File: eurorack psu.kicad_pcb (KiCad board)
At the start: 2 copper layers, 100 x 60 mm, 27 parts, among them J1 Screw Terminal 1x3, J2 Screw_Terminal_01x03, M3 MountingHole_3.2mm_M3_DIN965_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, U1 LM7812, U2 LM7912

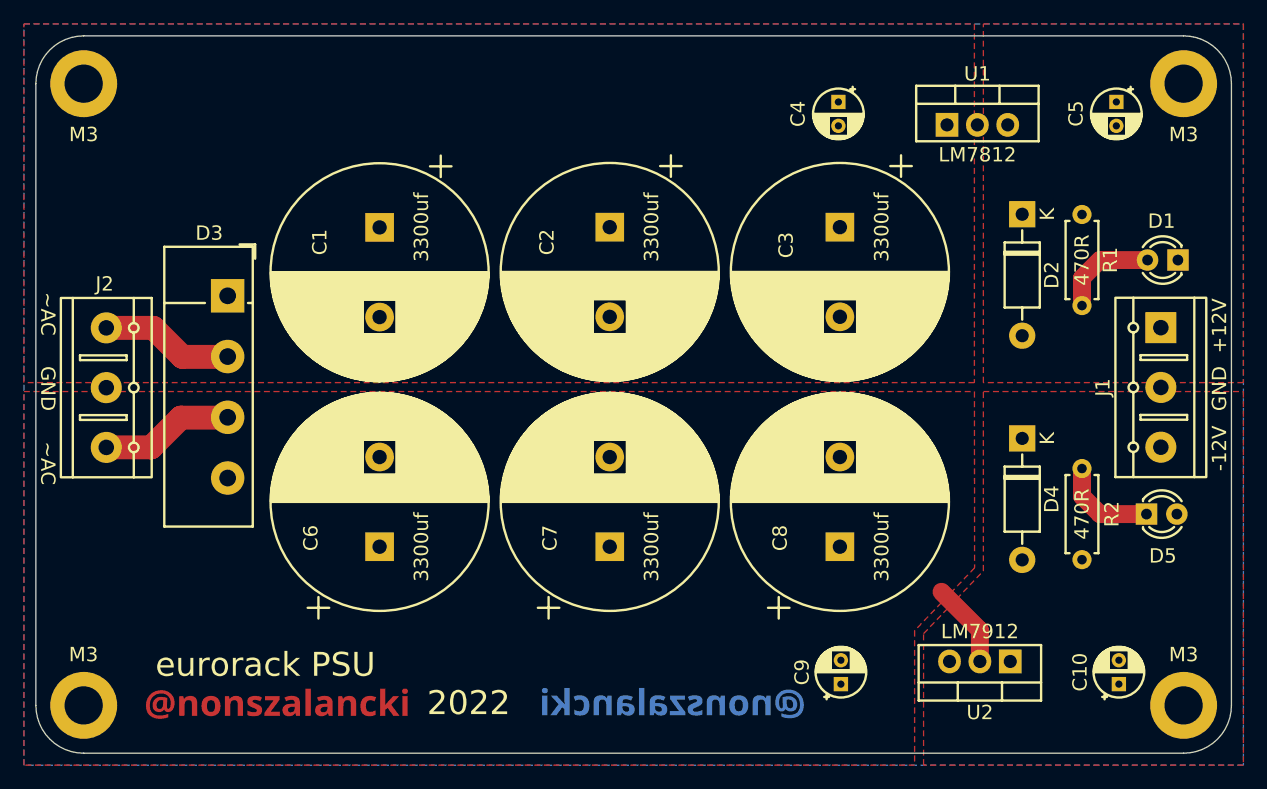
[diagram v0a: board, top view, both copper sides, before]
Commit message: added protection diode for 78xx & 79xx, corrected orientation of some parts
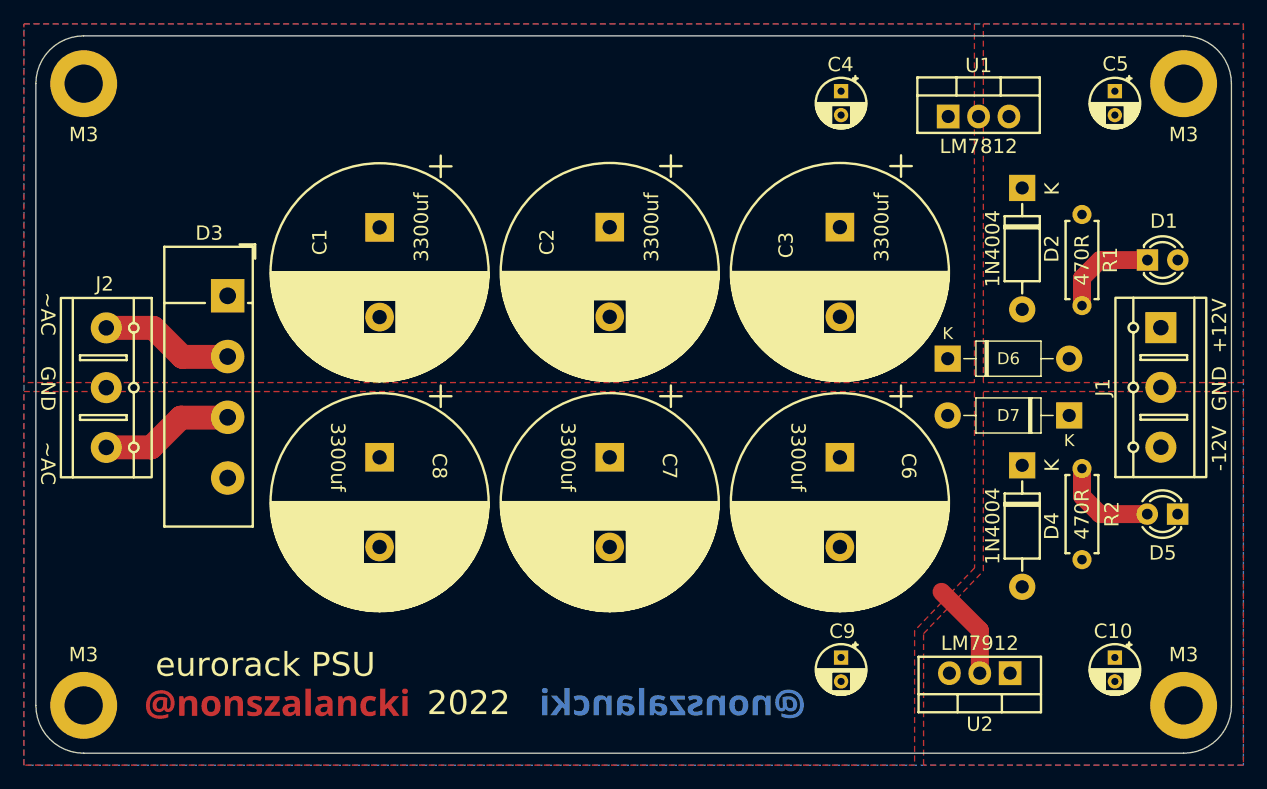
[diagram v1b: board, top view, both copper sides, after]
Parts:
- added D6: 1N4004, Diode_THT:D_DO-41_SOD81_P10.16mm_Horizontal, F.Cu at (108.3, 82.0)
- added D7: 1N4004, Diode_THT:D_DO-41_SOD81_P10.16mm_Horizontal, F.Cu at (118.4, 86.8)
- moved C6 39.2 mm to (99.2, 90.2), turned to -90 degrees
- moved C8 39.2 mm to (60.8, 90.2), turned to -90 degrees
- moved C7 7.48 mm to (80.0, 90.2), turned to -90 degrees
- moved D5 2.61 mm to (127.5, 95.0), turned to 180 degrees
- moved D1 2.55 mm to (125.0, 73.8), turned to 0 degrees
- moved C10 2.25 mm to (122.2, 107.0), turned to -90 degrees
- moved D4 2.25 mm to (114.5, 90.9)
- moved C9 2.23 mm to (99.3, 107.0), turned to -90 degrees
- moved D2 2.20 mm to (114.5, 67.7)
- moved U2 0.98 mm to (113.5, 108.3)
- moved C4 0.93 mm to (99.3, 59.6)
- moved C5 0.91 mm to (122.2, 59.6)
- moved U1 0.71 mm to (108.3, 61.7)
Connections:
- C10 pad 1: -12V -> GND
- C10 pad 2: GND -> -12V
- C6 pad 1: /L1 -> GND
- C6 pad 2: GND -> /L1
- C7 pad 1: /L1 -> GND
- C7 pad 2: GND -> /L1
- C8 pad 1: /L1 -> GND
- C8 pad 2: GND -> /L1
- C9 pad 1: /L1 -> GND
- C9 pad 2: GND -> /L1
- D1 pad 1: GND -> Net-(D1-Pad1)
- D1 pad 2: Net-(D1-Pad2) -> GND
- D5 pad 1: Net-(D5-Pad1) -> GND
- D5 pad 2: GND -> Net-(D5-Pad2)
- R1 pad 2: Net-(D1-Pad2) -> Net-(D1-Pad1)
- R2 pad 2: Net-(D5-Pad1) -> Net-(D5-Pad2)
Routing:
- net Net-(D1-Pad2): track 8.42 -> 0.00 mm
- net Net-(D1-Pad1): track 0.00 -> 8.42 mm
- net Net-(D5-Pad2): track 0.00 -> 8.33 mm
- net Net-(D5-Pad1): track 8.33 -> 0.00 mm
- net /L1: track 7.13 -> 8.13 mm

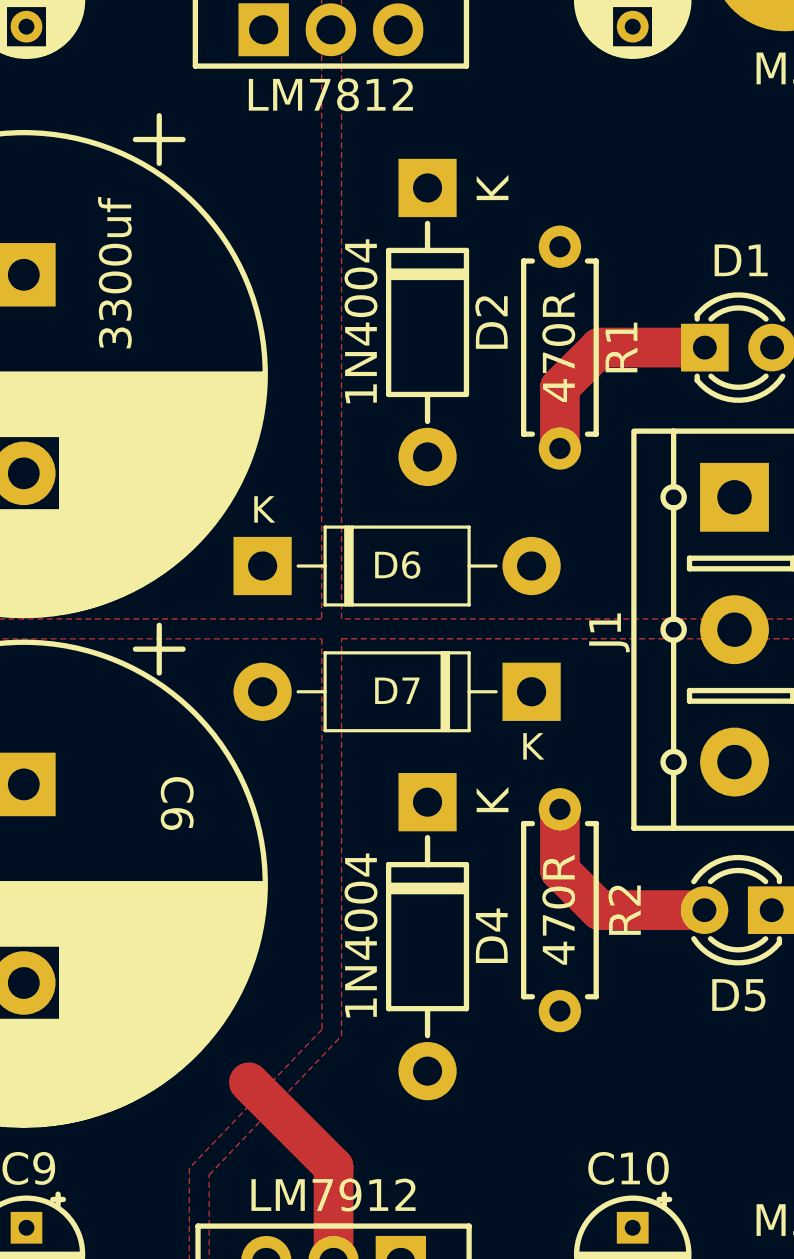
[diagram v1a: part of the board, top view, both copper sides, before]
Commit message: Updated parts placement
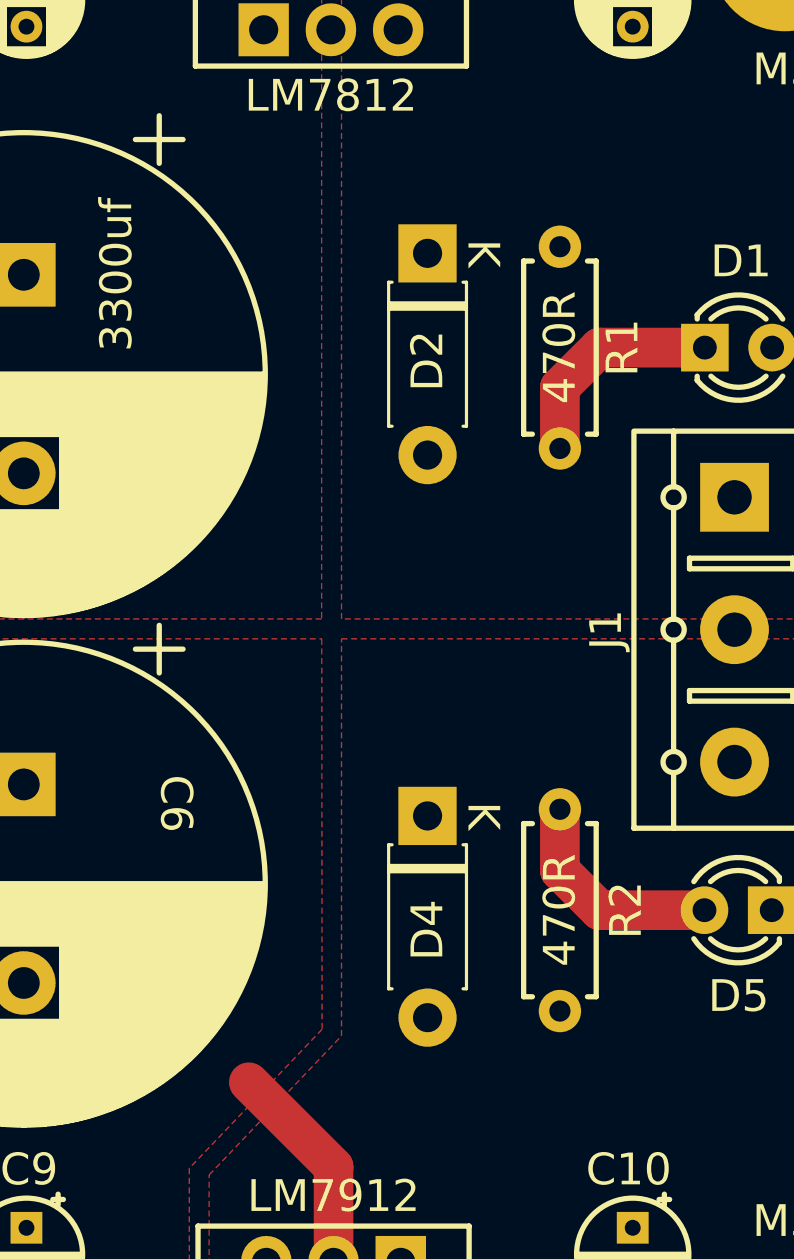
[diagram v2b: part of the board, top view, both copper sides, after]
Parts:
- removed D6, D7: 1N4004, Diode_THT:D_DO-41_SOD81_P10.16mm_Horizontal
- D2, D4: footprint Diode_THT:D_DO-41_SOD81_P10.16mm_Horizontal -> Diode_THT:D_DO-41_SOD81_P7.62mm_Horizontal
- moved D2 2.47 mm to (114.5, 70.2)
- moved D4 0.52 mm to (114.5, 91.4)
